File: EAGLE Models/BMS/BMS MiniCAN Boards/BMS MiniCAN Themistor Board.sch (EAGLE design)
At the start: 112 parts, among them IC1 AT90CAN128, IC2 MCP2551SO8, IC3 NUP2105L, Q1 56P2859, U1 0ZCH0050FF2G

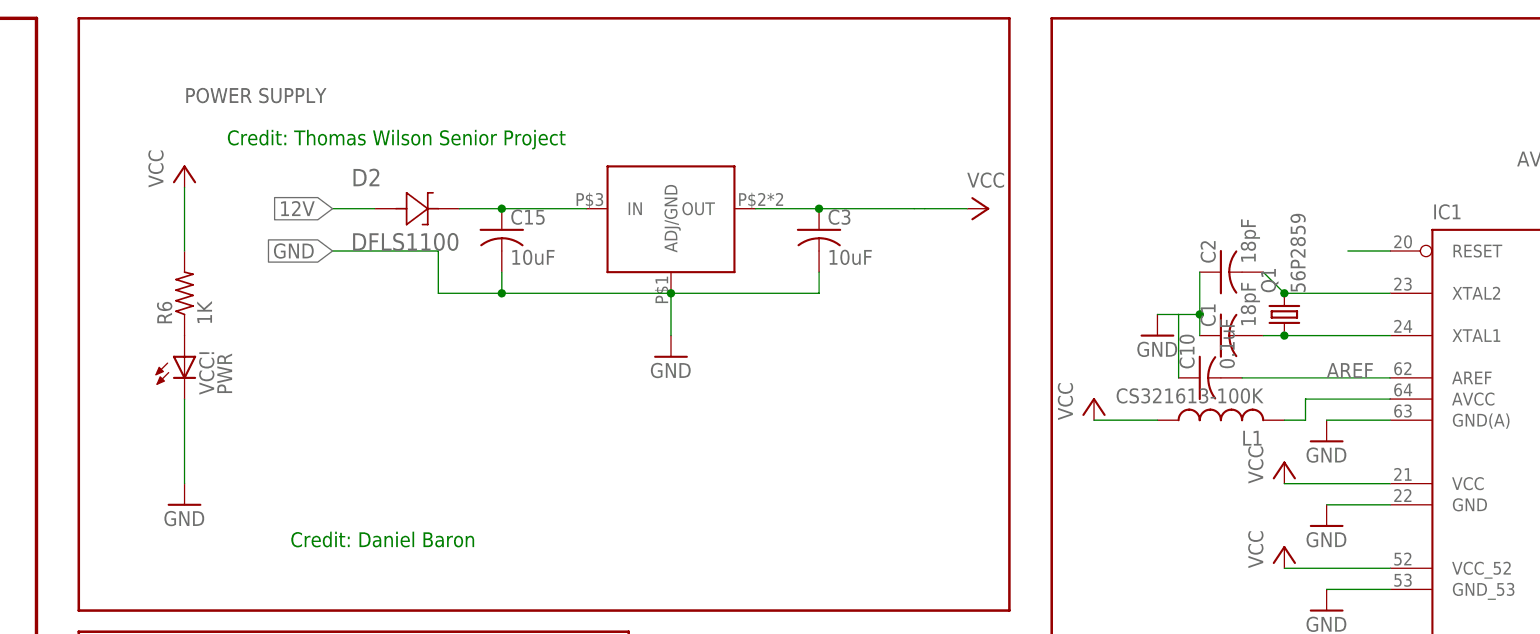
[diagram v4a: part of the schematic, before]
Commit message: Tilted MCU
Had everything traced out, but it didn't work, so retracing.
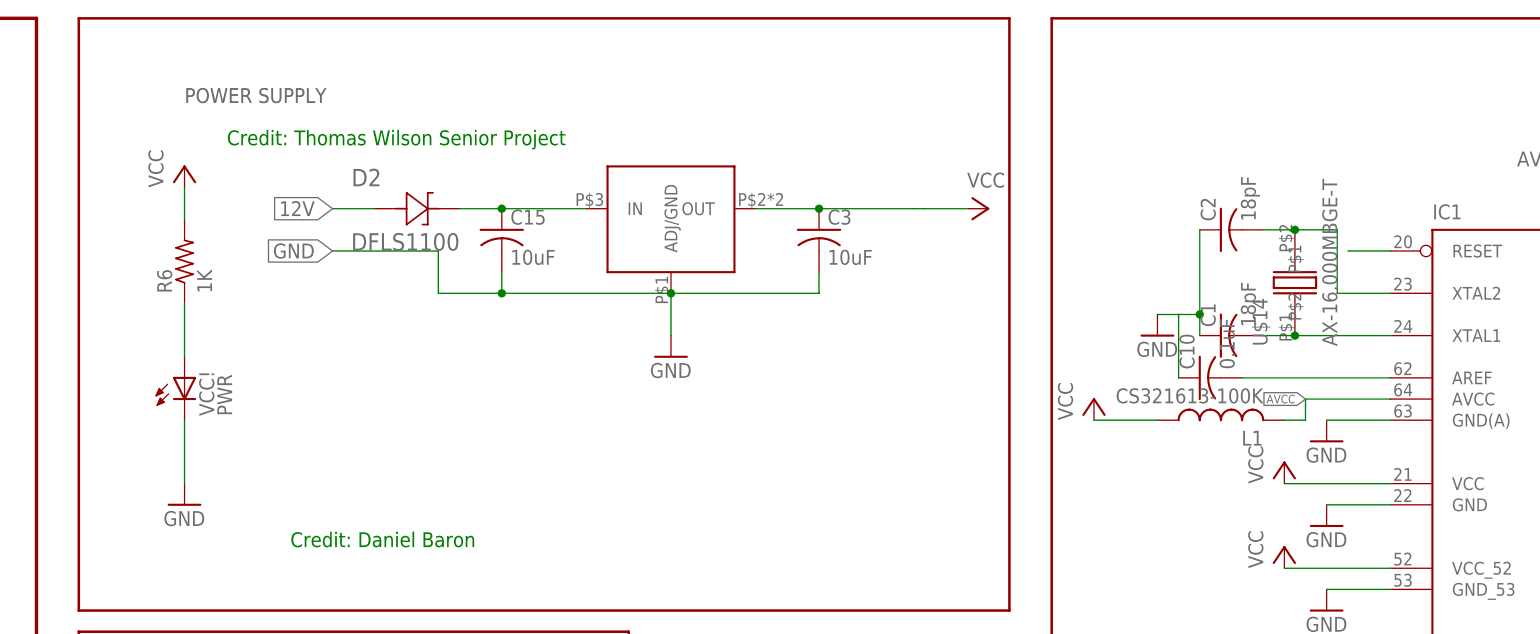
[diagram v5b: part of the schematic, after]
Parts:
- removed Q1: 56P2859, SparkFun-FreqCtrl:CRYSTALSMD
- added U$14: AX-16.000MBGE-T, BMS Lbr:AX-16.000MBGE-T
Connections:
- net N$2 renamed UF_GND
- removed net N$11: C1.2, IC1.XTAL1, Q1.1
- removed net N$3: C10.2, IC1.AREF
- new net AVCC: IC1.AVCC, L1.2
- new net XTAL2: C2.2, IC1.XTAL2, U$14.P$2
- net AREF: now also C10.2, IC1.AREF; no longer IC1.AVCC, L1.2
- net XTAL1: now also C1.2, IC1.XTAL1, U$14.P$1; no longer C2.2, IC1.XTAL2, Q1.2
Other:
- moved on the sheet: C2, R6, VCC!
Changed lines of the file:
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@@
 <setting verticaltext="up"/>
 </settings>
-<grid distance="0.1" unitdist="inch" unit="inch" style="lines" multiple="1" display="no" altdistance="0.01" altunitdist="inch" altunit="inch"/>
+<grid distance="1.27" unitdist="mm" unit="mm" style="lines" multiple="1" display="no" altdistance="0.3175" altunitdist="mm" altunit="mm"/>
 <layers>
 <layer number="1" name="Top" color="4" fill="1" visible="no" active="no"/>
@@
 <part name="IC1" library="at90can128" deviceset="AT90CAN128" device=""/>
 <part name="IC2" library="can" deviceset="MCP2551" device="SO8"/>
-<part name="Q1" library="SparkFun-FreqCtrl" deviceset="CRYSTAL" device="SMD" value="56P2859"/>
 <part name="C2" library="rcl" deviceset="C-US" device="C0805" value="18pF"/>
 <part name="C1" library="rcl" deviceset="C-US" device="C0805" value="18pF"/>
@@
 <part name="ISP1" library="adafruit" deviceset="AVRISP" device="-6"/>
 <part name="C10" library="rcl" deviceset="C-US" device="C0805" value="0.1uF"/>
+<part name="U$14" library="BMS Lbr" deviceset="AX-16.000MBGE-T" device=""/>
 </parts>
 <sheets>
@@
 <instance part="IC1" gate="G$1" x="365.76" y="114.3"/>
 <instance part="IC2" gate="G$1" x="187.96" y="58.42"/>
-<instance part="Q1" gate="G$1" x="304.8" y="167.64" rot="R90"/>
-<instance part="C2" gate="G$1" x="297.18" y="172.72" rot="R90"/>
+<instance part="C2" gate="G$1" x="297.18" y="177.8" rot="R90"/>
 <instance part="C1" gate="G$1" x="297.18" y="165.1" rot="R90"/>
 <instance part="GND1" gate="1" x="289.56" y="165.1"/>
@@
 <instance part="D1" gate="G$1" x="208.28" y="111.76" rot="R90"/>
 <instance part="GND9" gate="1" x="200.66" y="96.52"/>
-<instance part="VCC!" gate="G$1" x="172.72" y="162.56"/>
-<instance part="R6" gate="G$1" x="172.72" y="170.18" rot="R90"/>
+<instance part="VCC!" gate="G$1" x="172.72" y="160.02"/>
+<instance part="R6" gate="G$1" x="172.72" y="173.99" rot="R90"/>
 <instance part="GND10" gate="1" x="309.88" y="132.08"/>
 <instance part="GND11" gate="1" x="309.88" y="142.24"/>
@@
 <instance part="ISP1" gate="G$1" x="120.65" y="19.05"/>
 <instance part="C10" gate="G$1" x="294.64" y="160.02" rot="R90"/>
+<instance part="U$14" gate="G$1" x="306.07" y="171.45" rot="R90"/>
 </instances>
 <busses>
@@
 </segment>
 <segment>
-<wire x1="172.72" y1="182.88" x2="172.72" y2="175.26" width="0.1524" layer="91"/>
+<wire x1="172.72" y1="182.88" x2="172.72" y2="179.07" width="0.1524" layer="91"/>
 <pinref part="P+3" gate="VCC" pin="VCC"/>
 <pinref part="R6" gate="G$1" pin="2"/>
@@
 <net name="GND" class="0">
 <segment>
-<wire x1="172.72" y1="147.32" x2="172.72" y2="157.48" width="0.1524" layer="91"/>
+<wire x1="172.72" y1="147.32" x2="172.72" y2="154.94" width="0.1524" layer="91"/>
 <pinref part="GND8" gate="1" pin="GND"/>
 <pinref part="VCC!" gate="G$1" pin="C"/>
@@
 </segment>
 <segment>
-<wire x1="294.64" y1="172.72" x2="294.64" y2="167.64" width="0.1524" layer="91"/>
+<wire x1="294.64" y1="177.8" x2="294.64" y2="167.64" width="0.1524" layer="91"/>
 <wire x1="294.64" y1="165.1" x2="294.64" y2="167.64" width="0.1524" layer="91"/>
 <wire x1="294.64" y1="167.64" x2="292.1" y2="167.64" width="0.1524" layer="91"/>
@@
 </segment>
 </net>
-<net name="XTAL1" class="0">
-<segment>
-<wire x1="304.8" y1="170.18" x2="317.5" y2="170.18" width="0.1524" layer="91"/>
-<wire x1="304.8" y1="170.18" x2="302.26" y2="172.72" width="0.1524" layer="91"/>
-<junction x="304.8" y="170.18"/>
-<pinref part="IC1" gate="G$1" pin="XTAL2"/>
-<pinref part="Q1" gate="G$1" pin="2"/>
-<pinref part="C2" gate="G$1" pin="2"/>
-</segment>
-</net>
 <net name="RESET" class="0">
 <segment>
@@
 </segment>
 </net>
-<net name="AREF" class="0">
+<net name="AVCC" class="0">
 <segment>
-<label x="309.88" y="160.02" size="1.778" layer="95"/>
 <pinref part="L1" gate="G$1" pin="2"/>
 <wire x1="304.8" y1="154.94" x2="307.34" y2="154.94" width="0.1524" layer="91"/>
@@
 <pinref part="IC1" gate="G$1" pin="AVCC"/>
 <wire x1="307.34" y1="157.48" x2="317.5" y2="157.48" width="0.1524" layer="91"/>
+<label x="307.34" y="157.48" size="1.016" layer="95" rot="R180" xref="yes"/>
 </segment>
 </net>
@@
 </segment>
 </net>
-<net name="N$11" class="0">
-<segment>
-<wire x1="304.8" y1="165.1" x2="317.5" y2="165.1" width="0.1524" layer="91"/>
-<wire x1="304.8" y1="165.1" x2="302.26" y2="165.1" width="0.1524" layer="91"/>
-<junction x="304.8" y="165.1"/>
-<pinref part="Q1" gate="G$1" pin="1"/>
-<pinref part="IC1" gate="G$1" pin="XTAL1"/>
-<pinref part="C1" gate="G$1" pin="2"/>
-</segment>
-</net>
 <net name="N$9" class="0">
 <segment>
 <pinref part="VCC!" gate="G$1" pin="A"/>
 <pinref part="R6" gate="G$1" pin="1"/>
+<wire x1="172.72" y1="162.56" x2="172.72" y2="168.91" width="0.1524" layer="91"/>
 </segment>
 </net>
@@
 </segment>
 </net>
-<net name="N$2" class="0">
+<net name="UF_GND" class="0">
 <segment>
 <pinref part="U1" gate="A" pin="1"/>
@@
 </segment>
 </net>
-<net name="N$3" class="0">
+<net name="AREF" class="0">
 <segment>
 <pinref part="C10" gate="G$1" pin="2"/>
@@
 </segment>
 </net>
+<net name="XTAL2" class="0">
+<segment>
+<pinref part="C2" gate="G$1" pin="2"/>
+<pinref part="U$14" gate="G$1" pin="P$2"/>
+<wire x1="302.26" y1="177.8" x2="306.07" y2="177.8" width="0.1524" layer="91"/>
+<wire x1="306.07" y1="177.8" x2="311.15" y2="177.8" width="0.1524" layer="91"/>
+<wire x1="311.15" y1="177.8" x2="311.15" y2="170.18" width="0.1524" layer="91"/>
+<junction x="306.07" y="177.8"/>
+<pinref part="IC1" gate="G$1" pin="XTAL2"/>
+<wire x1="311.15" y1="170.18" x2="317.5" y2="170.18" width="0.1524" layer="91"/>
+</segment>
+</net>
+<net name="XTAL1" class="0">
+<segment>
+<pinref part="C1" gate="G$1" pin="2"/>
+<pinref part="U$14" gate="G$1" pin="P$1"/>
+<wire x1="302.26" y1="165.1" x2="306.07" y2="165.1" width="0.1524" layer="91"/>
+<pinref part="IC1" gate="G$1" pin="XTAL1"/>
+<wire x1="306.07" y1="165.1" x2="317.5" y2="165.1" width="0.1524" layer="91"/>
+<junction x="306.07" y="165.1"/>
+</segment>
+</net>

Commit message: Finished First Revision of Thermistor Board
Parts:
- ISP1: value AVRISP-6 -> 95278; device adafruit:AVRISP-6 -> con-amphenol:95278
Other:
- moved on the sheet: ISP1
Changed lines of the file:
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@@
 <setting verticaltext="up"/>
 </settings>
-<grid distance="1.27" unitdist="mm" unit="mm" style="lines" multiple="1" display="no" altdistance="0.3175" altunitdist="mm" altunit="mm"/>
+<grid distance="0.1" unitdist="inch" unit="inch" style="lines" multiple="1" display="no" altdistance="0.01" altunitdist="inch" altunit="inch"/>
 <layers>
 <layer number="1" name="Top" color="4" fill="1" visible="no" active="no"/>
@@
 <part name="D2" library="BMS Lbr" deviceset="DFLS1100" device=""/>
 <part name="U$13" library="BMS Lbr" deviceset="0039300040" device=""/>
-<part name="ISP1" library="adafruit" deviceset="AVRISP" device="-6"/>
 <part name="C10" library="rcl" deviceset="C-US" device="C0805" value="0.1uF"/>
 <part name="U$14" library="BMS Lbr" deviceset="AX-16.000MBGE-T" device=""/>
+<part name="ISP1" library="con-amphenol" deviceset="95278" device=""/>
 </parts>
 <sheets>
@@
 <instance part="D2" gate="G$1" x="195.58" y="180.34"/>
 <instance part="U$13" gate="G$1" x="81.28" y="55.88" rot="R180"/>
-<instance part="ISP1" gate="G$1" x="120.65" y="19.05"/>
 <instance part="C10" gate="G$1" x="294.64" y="160.02" rot="R90"/>
 <instance part="U$14" gate="G$1" x="306.07" y="171.45" rot="R90"/>
+<instance part="ISP1" gate="G$1" x="121.666" y="19.05"/>
 </instances>
 <busses>
@@
 </segment>
 <segment>
+<label x="139.7" y="21.59" size="1.778" layer="95"/>
 <pinref part="ISP1" gate="G$1" pin="VCC"/>
-<wire x1="135.89" y1="21.59" x2="139.7" y2="21.59" width="0.1524" layer="91"/>
-<label x="139.7" y="21.59" size="1.778" layer="95"/>
+<wire x1="131.826" y1="21.59" x2="139.7" y2="21.59" width="0.1524" layer="91"/>
 </segment>
 <segment>
@@
 </segment>
 <segment>
+<label x="139.7" y="16.51" size="1.778" layer="95"/>
 <pinref part="ISP1" gate="G$1" pin="GND"/>
-<wire x1="135.89" y1="16.51" x2="139.7" y2="16.51" width="0.1524" layer="91"/>
-<label x="139.7" y="16.51" size="1.778" layer="95"/>
+<wire x1="131.826" y1="16.51" x2="139.7" y2="16.51" width="0.1524" layer="91"/>
 </segment>
 </net>
@@
 </segment>
 <segment>
+<wire x1="111.506" y1="16.51" x2="104.14" y2="16.51" width="0.1524" layer="91"/>
+<label x="96.52" y="16.51" size="1.778" layer="95"/>
 <pinref part="ISP1" gate="G$1" pin="RST"/>
-<wire x1="107.95" y1="16.51" x2="104.14" y2="16.51" width="0.1524" layer="91"/>
-<label x="96.52" y="16.51" size="1.778" layer="95"/>
 </segment>
 </net>
@@
 </segment>
 <segment>
+<label x="139.7" y="19.05" size="1.778" layer="95"/>
 <pinref part="ISP1" gate="G$1" pin="MOSI"/>
-<wire x1="135.89" y1="19.05" x2="139.7" y2="19.05" width="0.1524" layer="91"/>
-<label x="139.7" y="19.05" size="1.778" layer="95"/>
+<wire x1="131.826" y1="19.05" x2="139.7" y2="19.05" width="0.1524" layer="91"/>
 </segment>
 </net>
@@
 </segment>
 <segment>
+<wire x1="111.506" y1="21.59" x2="104.14" y2="21.59" width="0.1524" layer="91"/>
+<label x="101.6" y="21.59" size="1.778" layer="95"/>
 <pinref part="ISP1" gate="G$1" pin="MISO"/>
-<wire x1="107.95" y1="21.59" x2="104.14" y2="21.59" width="0.1524" layer="91"/>
-<label x="101.6" y="21.59" size="1.778" layer="95"/>
 </segment>
 </net>
@@
 </segment>
 <segment>
+<wire x1="111.506" y1="19.05" x2="104.14" y2="19.05" width="0.1524" layer="91"/>
+<label x="92.71" y="19.05" size="1.778" layer="95"/>
 <pinref part="ISP1" gate="G$1" pin="SCK"/>
-<wire x1="107.95" y1="19.05" x2="104.14" y2="19.05" width="0.1524" layer="91"/>
-<label x="92.71" y="19.05" size="1.778" layer="95"/>
-</segment>
-</net>
+</segment>
+</net>
